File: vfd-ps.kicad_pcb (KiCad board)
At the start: 2 copper layers, 58 x 45 mm, 48 parts, among them J1 Conn_01x04, J2 Conn_01x04, J3 Conn_01x04, U1 TPS54360DDA, U2 LM4871

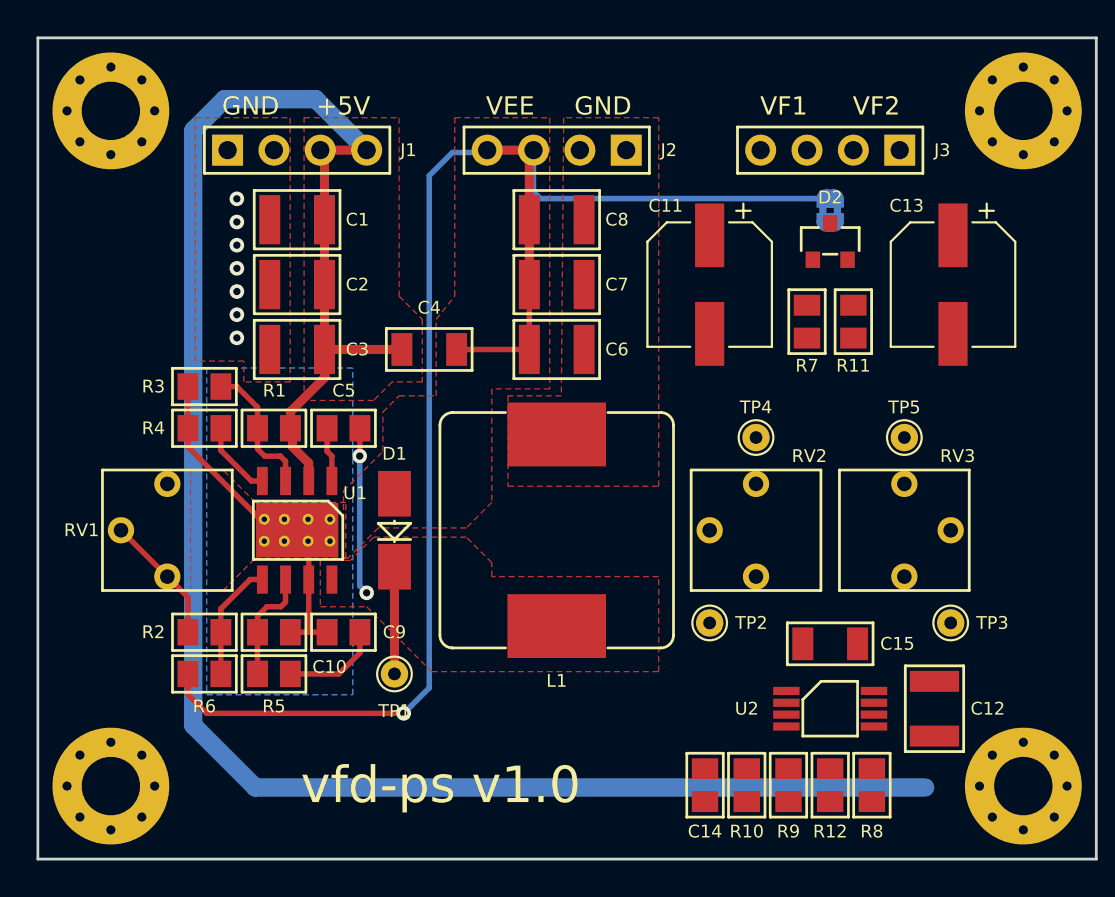
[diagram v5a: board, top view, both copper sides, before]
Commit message: Trace all pcb nets
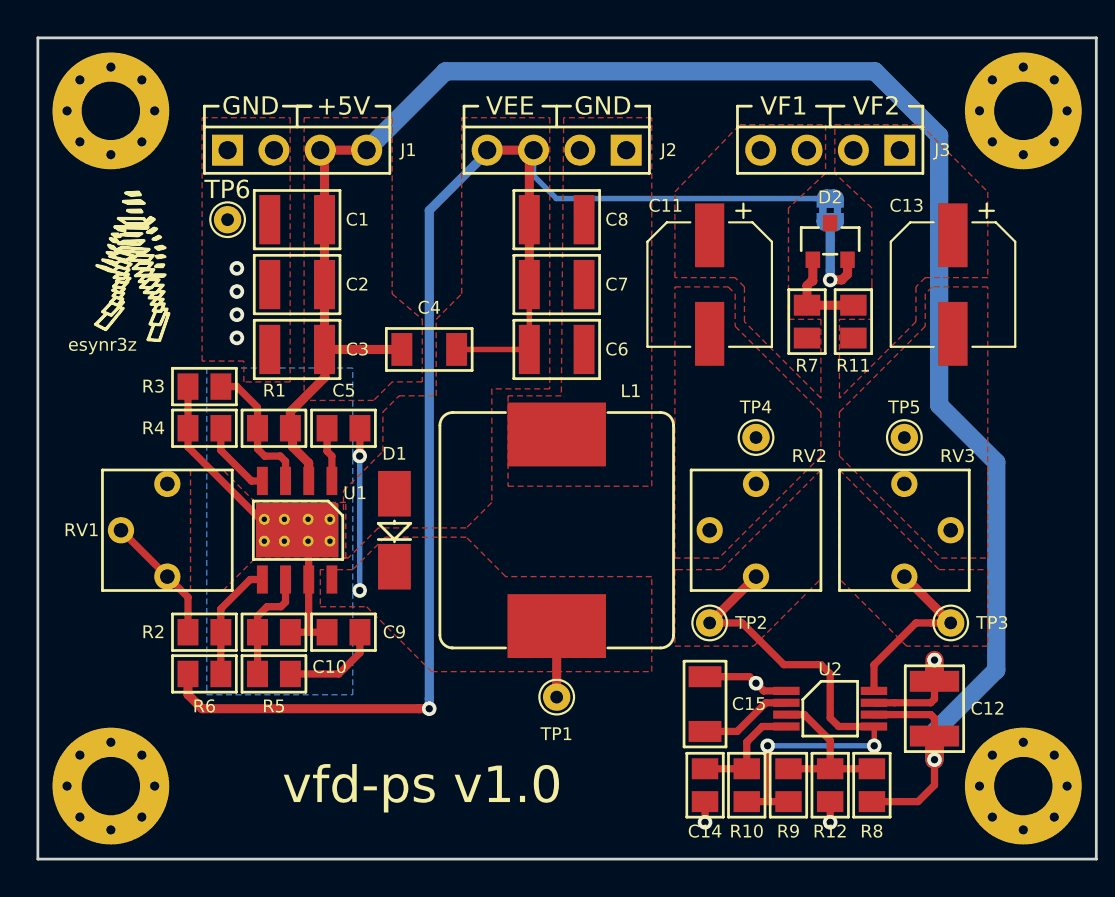
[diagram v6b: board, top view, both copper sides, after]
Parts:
- added G***: LOGO, esynr3z_Symbol:esynr3z_logo_4.5x8.4mm_Silk, F.Cu at (123.1, 87.5)
- added TP6: TestPoint, esynr3z_TestPoint:TestPoint_THTPad_D1.5mm_Drill0.7mm, F.Cu at (128.4, 85.0)
- moved TP1 8.98 mm to (146.4, 111.1)
- moved C15 7.61 mm to (154.6, 111.5), turned to 90 degrees
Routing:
- net Net-(R10-Pad2): track 0.00 -> 29.7 mm, vias 0 -> 2
- net GND: track 0.00 -> 12.6 mm, vias 7 -> 8
- net Net-(RV3-Pad1): track 0.00 -> 10.2 mm
- net Net-(R12-Pad1): track 0.00 -> 9.11 mm
- net Net-(C14-Pad1): track 0.00 -> 6.28 mm
- net Net-(D2-Pad1): track 0.00 -> 5.21 mm
- net Net-(C15-Pad1): track 0.00 -> 5.11 mm
- net Net-(D2-Pad2): track 0.00 -> 4.98 mm, vias 0 -> 1
- net +5V: track 111.7 -> 108.6 mm, vias 0 -> 1
- net Net-(C5-Pad2): track 15.1 -> 12.8 mm
- net GNDPAD: track 99.5 -> 98.3 mm
- added copper zone on F.Cu, net Net-(C11-Pad2)
- added copper zone on F.Cu, net Net-(C13-Pad2)
- added copper zone on F.Cu, net Net-(R10-Pad2)
- added copper zone on F.Cu, net Net-(RV3-Pad1)
- added copper zone on F.Cu, net VF1
- added copper zone on F.Cu, net VF2
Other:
- board text added: "esynr3z"

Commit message: Add image to silk
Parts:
- added G***: LOGO, esynr3z_Symbol:iv18_draw, B.Cu at (146.8, 97.3)

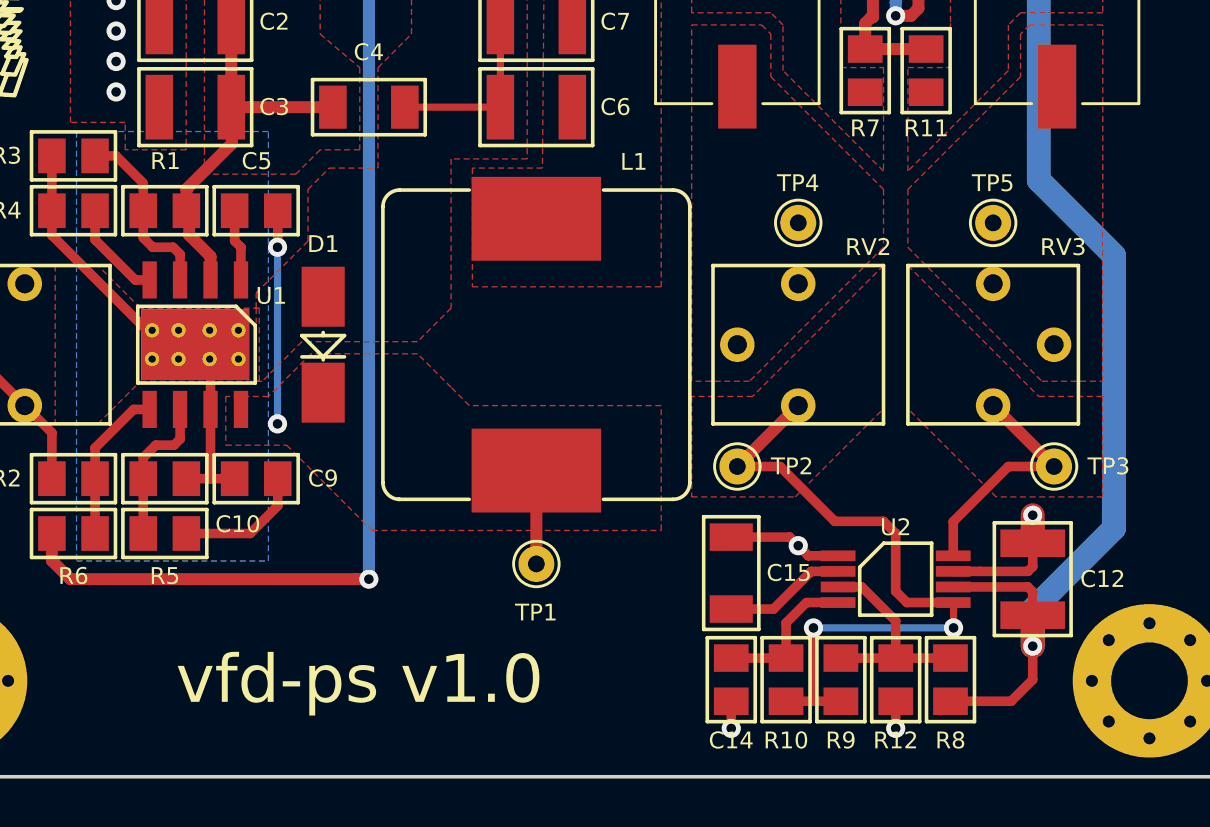
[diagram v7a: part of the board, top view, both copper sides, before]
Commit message: Some minor silk fixes
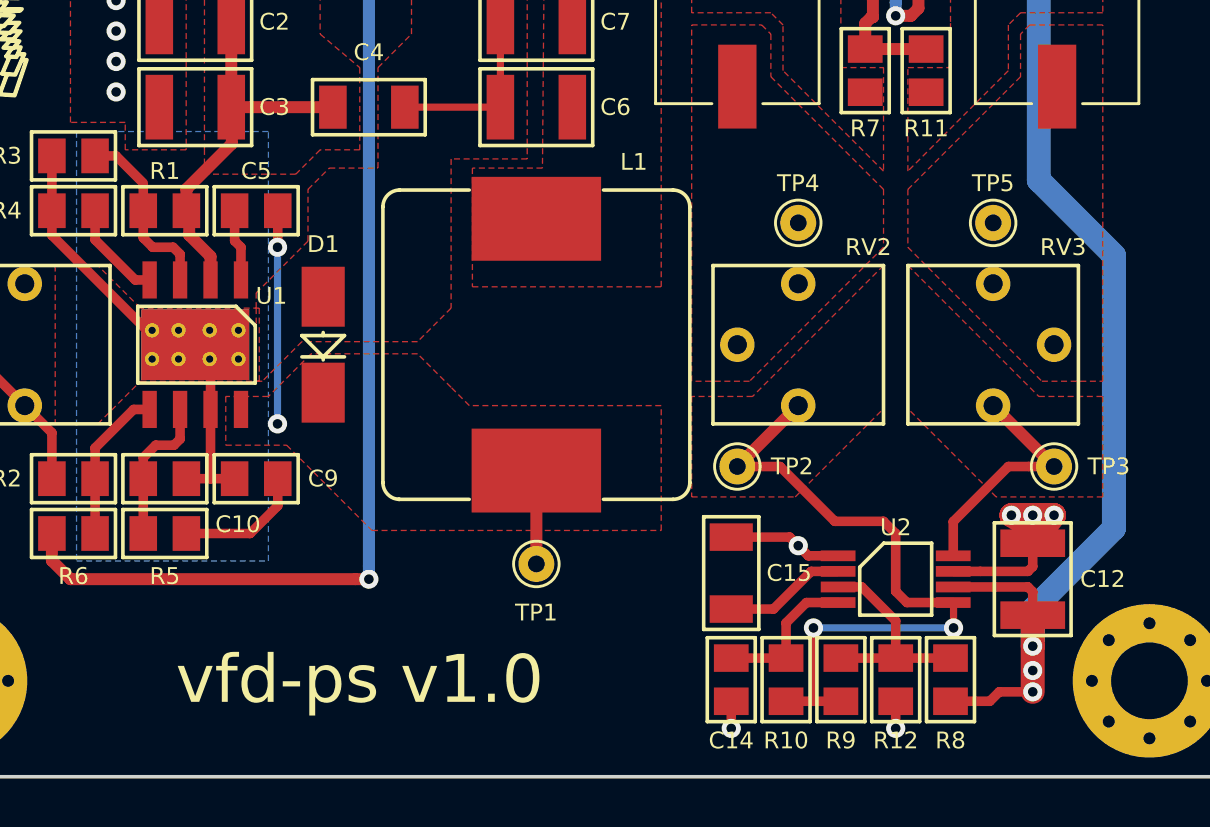
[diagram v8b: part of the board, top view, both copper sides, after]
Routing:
- net GND: track 12.6 -> 18.5 mm, vias 8 -> 10
- net +5V: track 108.6 -> 108.9 mm, vias 1 -> 3
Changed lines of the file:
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@@
-(kicad_pcb (version 20171130) (host pcbnew 6.0.0-rc1-unknown-r13424-46f5d81d)
+(kicad_pcb (version 20171130) (host pcbnew 6.0.0-rc1-unknown-r13783-618182dc)
   (general
     (thickness 1.6)
     (drawings 36)
-    (tracks 165)
+    (tracks 175)
     (zones 0)
     (modules 51)
@@
     (37 F.SilkS user)
     (38 B.Mask user hide)
-    (39 F.Mask user)
+    (39 F.Mask user hide)
     (40 Dwgs.User user)
     (44 Edge.Cuts user)
@@
     (pad_drill 0.762)
     (pad_to_mask_clearance 0.2)
+    (solder_mask_min_width 0.25)
     (aux_axis_origin 0 0)
     (visible_elements 7FFFFFFF)
@@
     (tags "resistor 0805")
     (attr smd)
-    (fp_text reference R1 (at -0.026 2.063) (layer F.SilkS)
+    (fp_text reference R1 (at 0 1.651) (layer F.SilkS)
       (effects (font (size 0.7 0.7) (thickness 0.15)))
     )
@@
     (tags "capacitor 0805")
     (attr smd)
-    (fp_text reference C5 (at 0.026 -2.063 180) (layer F.SilkS)
+    (fp_text reference C5 (at 0 -1.651 180) (layer F.SilkS)
       (effects (font (size 0.7 0.7) (thickness 0.15)))
     )
@@
   (segment (start 154.559 110.006) (end 156.996 110.006) (width 0.4) (layer F.Cu) (net 1))
   (via (at 167.132002 109.093) (size 0.8) (drill 0.4) (layers F.Cu B.Cu) (net 1))
-  (segment (start 167.132002 110.259998) (end 167.132002 109.658685) (width 1) (layer F.Cu) (net 1))
-  (segment (start 167.132002 109.658685) (end 167.132002 109.093) (width 1) (layer F.Cu) (net 1))
+  (segment (start 167.132002 110.259998) (end 168.021 109.093) (width 1) (layer F.Cu) (net 1))
+  (segment (start 167.132002 109.658685) (end 166.243 109.093) (width 1) (layer F.Cu) (net 1))
   (segment (start 167.132 110.26) (end 167.132002 110.259998) (width 1) (layer F.Cu) (net 1))
+  (segment (start 167.132002 109.093) (end 168.021 109.093) (width 1) (layer F.Cu) (net 1))
+  (segment (start 168.021 109.093) (end 166.243 109.093) (width 1) (layer F.Cu) (net 1))
+  (segment (start 168.021 109.093) (end 167.132002 109.658685) (width 1) (layer F.Cu) (net 1))
+  (via (at 168.021 109.093) (size 0.8) (drill 0.4) (layers F.Cu B.Cu) (net 1))
+  (segment (start 166.243 109.093) (end 167.132002 109.093) (width 1) (layer F.Cu) (net 1))
+  (via (at 166.243 109.093) (size 0.8) (drill 0.4) (layers F.Cu B.Cu) (net 1))
   (segment (start 131.953 96.647) (end 131.837 96.531) (width 0.5) (layer F.Cu) (net 2))
   (segment (start 131.837 96.531) (end 131.837 96.393) (width 0.5) (layer F.Cu) (net 2))
@@
   (segment (start 170.518001 98.255001) (end 170.518001 109.643999) (width 1) (layer B.Cu) (net 2))
   (segment (start 167.132 113.26) (end 167.132 114.554) (width 1) (layer F.Cu) (net 2))
-  (segment (start 167.132 115.951) (end 167.132 114.554) (width 0.4) (layer F.Cu) (net 2))
-  (segment (start 163.703 116.851) (end 166.232 116.851) (width 0.4) (layer F.Cu) (net 2))
-  (segment (start 166.232 116.851) (end 167.132 115.951) (width 0.4) (layer F.Cu) (net 2))
+  (via (at 167.132 115.57) (size 0.8) (drill 0.4) (layers F.Cu B.Cu) (net 2))
+  (segment (start 167.132 114.554) (end 167.132 116.458996) (width 1) (layer F.Cu) (net 2))
+  (segment (start 167.131996 116.459) (end 167.132 116.458996) (width 0.4) (layer F.Cu) (net 2))
+  (via (at 167.132 116.458996) (size 0.8) (drill 0.4) (layers F.Cu B.Cu) (net 2))
+  (segment (start 165.735 116.459) (end 167.131996 116.459) (width 0.4) (layer F.Cu) (net 2))
+  (segment (start 163.703 116.851) (end 165.343 116.851) (width 0.4) (layer F.Cu) (net 2))
+  (segment (start 165.343 116.851) (end 165.735 116.459) (width 0.4) (layer F.Cu) (net 2))
   (segment (start 142.621 81.153) (end 145.161 81.153) (width 0.5) (layer F.Cu) (net 3))
   (segment (start 144.931 81.383) (end 145.161 81.153) (width 0.5) (layer F.Cu) (net 3))
